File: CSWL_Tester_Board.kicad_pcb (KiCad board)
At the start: 2 copper layers, 72.3 x 72.3 mm, 56 parts, among them J1 Conn_02x10_Odd_Even, J2 Conn_02x10_Odd_Even

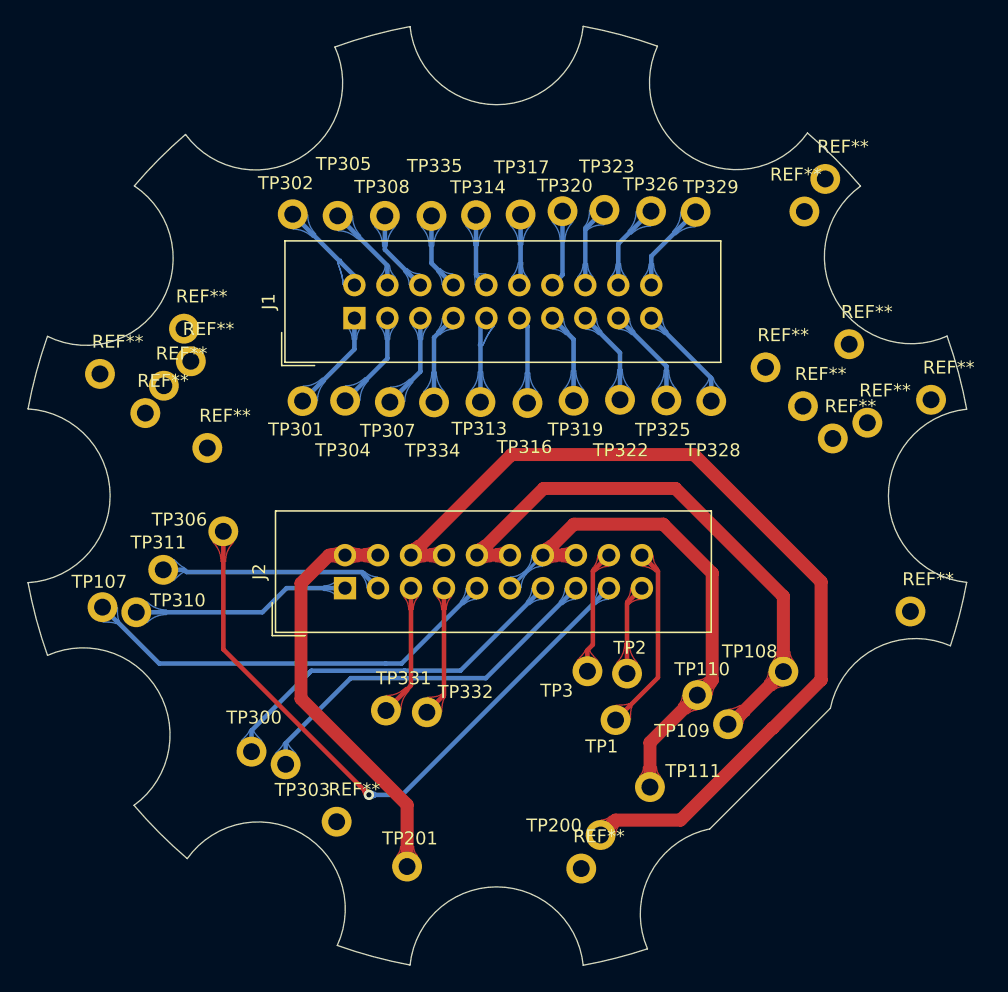
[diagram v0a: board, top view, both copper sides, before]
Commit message: Ruan: modify board shape
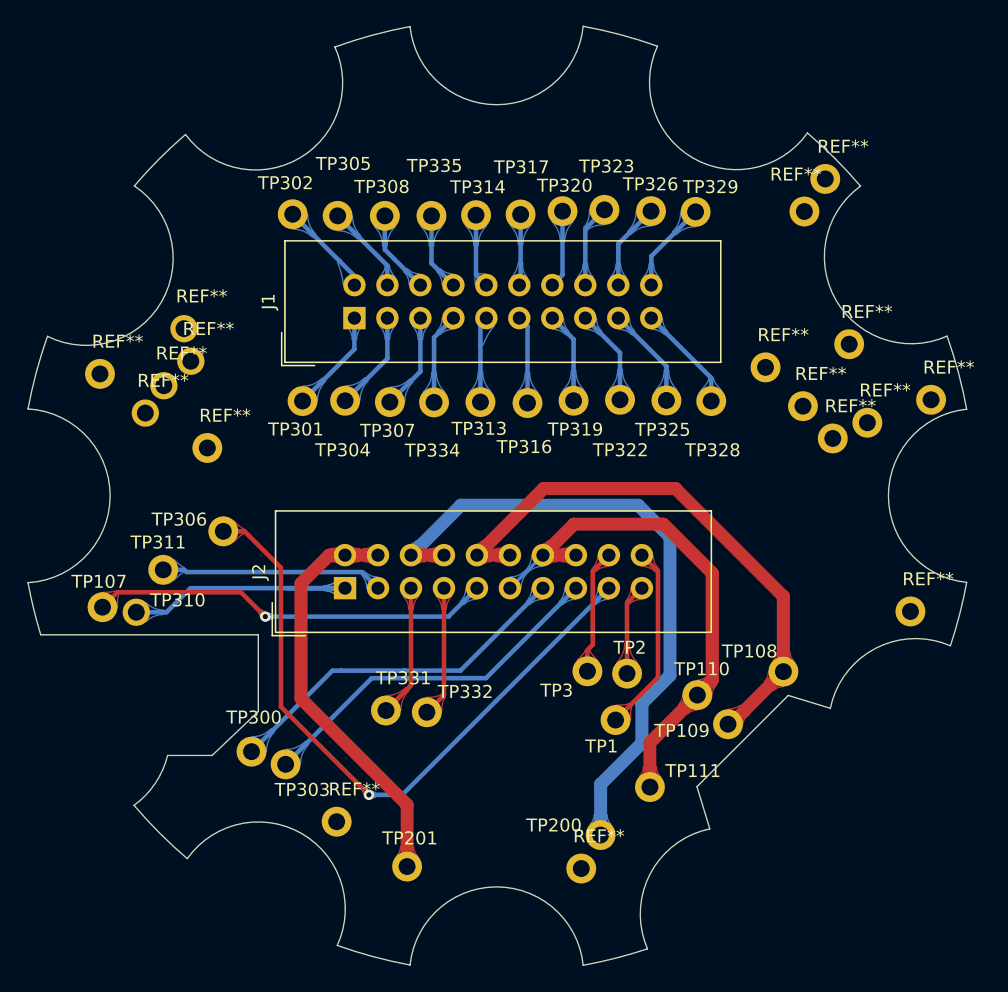
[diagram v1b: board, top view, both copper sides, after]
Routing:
- net /CSWL_Vout+: track 70.9 -> 50.2 mm
- net /TP300: track 40.7 -> 27.7 mm
- net /LED4+: track 16.8 -> 28.7 mm
- net /CSWL_VDD+: track 33.0 -> 31.3 mm, vias 0 -> 1
- net /TP306: track 50.0 -> 51.0 mm
- net /TP303: track 28.9 -> 28.0 mm
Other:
- outline, holes or cut-outs redrawn

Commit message: Ruan: extend the hold size to 1.7
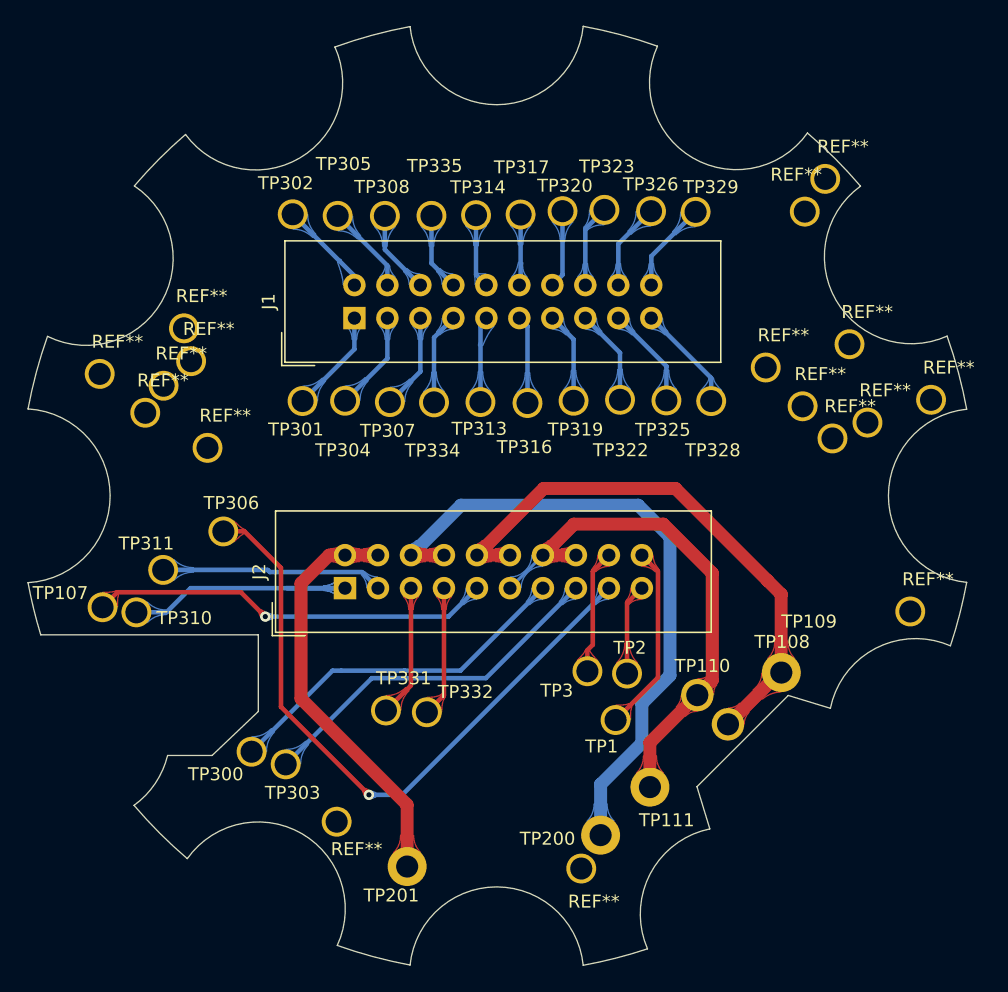
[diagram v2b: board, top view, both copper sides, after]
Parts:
- REF** (x17): value PinCard_Hole_D2.3mm_1.3dill -> PinCard_Hole_D2.3mm_1.5dill
- moved TP306 29.6 mm to (112.0, 113.7)
- moved TP311 28.4 mm to (107.4, 116.7)
- moved TP310 27.2 mm to (105.3, 119.9)
- moved TP107 24.0 mm to (102.7, 119.5)
- moved TP303 12.4 mm to (116.8, 131.6)
- moved TP110 11.0 mm to (148.5, 126.3)
- moved TP109 9.41 mm to (155.0, 124.6)
- moved TP108 7.76 mm to (150.9, 128.5)
- moved TP200 6.96 mm to (141.0, 137.1)
- moved TP201 4.62 mm to (126.2, 139.5)
- moved TP111 3.28 mm to (144.8, 133.4)
- moved TP300 3.26 mm to (114.2, 130.7)

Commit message: Ruan: V4.0 for MP1
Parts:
- moved TP110 3.24 mm to (147.1, 129.2)
- moved TP108 3.24 mm to (151.1, 125.3)
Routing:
- net /CSWL_IN-: track 40.2 -> 38.1 mm
- net /CSWL_IN+: track 43.5 -> 45.4 mm
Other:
- board text added: "V4.0 20191225"
